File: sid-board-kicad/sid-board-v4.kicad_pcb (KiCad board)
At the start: 2 copper layers, 52 parts, among them J1 SPI + UART, J2 USB_B_Micro, Q1 BSS138, Q2 BSS138, SW1 SW_EN, SW2 SW_FLASH, U1 SC16IS762IBS, U2 MCP1703A-3302_SOT223, U3 SN65HVD232, U4 SN65HVD232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

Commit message: Layer 4 stuff
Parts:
- removed the C8 at (139.6, 90.9)
- removed the C8 at (147.4, 90.9)
- removed D1: LED7, LED_SMD:LED_0805_2012Metric_Pad1.15x1.40mm_HandSolder
- removed D2: LED6, LED_SMD:LED_0805_2012Metric_Pad1.15x1.40mm_HandSolder
- removed D3: LED5, LED_SMD:LED_0805_2012Metric_Pad1.15x1.40mm_HandSolder
- removed D4: LED4, LED_SMD:LED_0805_2012Metric_Pad1.15x1.40mm_HandSolder
- removed D5: LED3, LED_SMD:LED_0805_2012Metric_Pad1.15x1.40mm_HandSolder
- removed D6: LED2, LED_SMD:LED_0805_2012Metric_Pad1.15x1.40mm_HandSolder
- removed D7: LED1, LED_SMD:LED_0805_2012Metric_Pad1.15x1.40mm_HandSolder
- removed D8: LED0, LED_SMD:LED_0805_2012Metric_Pad1.15x1.40mm_HandSolder
- removed J1: SPI + UART, Connector_PinHeader_2.00mm:PinHeader_2x05_P2.00mm_Vertical
- removed R18: 1K, Resistor_SMD:R_0805_2012Metric_Pad1.15x1.40mm_HandSolder
- added C8: 1uF, Capacitor_SMD:C_0805_2012Metric_Pad1.15x1.40mm_HandSolder, F.Cu at (108.6, 81.3)
- C2, C5, C9, D10, D11, U2, U3, U4, U7: moved to F.Cu
- moved I-BUS1 71.2 mm to (117.5, 141.0), turned to 90 degrees
- moved H3 69.7 mm to (109.2, 71.1)
- moved H1 65.5 mm to (154.9, 116.8)
- moved R5 63.1 mm to (201.8, 94.9), turned to 0 degrees
- moved R4 56.1 mm to (194.7, 100.9), turned to 0 degrees
- moved H2 56.0 mm to (154.9, 71.1)
- moved C6 55.7 mm to (194.8, 106.8)
- moved U7 55.1 mm to (127.0, 138.4), turned to 180 degrees
- moved R6 52.2 mm to (190.2, 90.0)
- moved R2 50.8 mm to (190.1, 105.9), turned to 0 degrees
- moved J2 50.5 mm to (132.1, 119.4), turned to 0 degrees
- moved C5 49.4 mm to (126.8, 133.3)
- moved R3 46.1 mm to (185.3, 109.0), turned to 0 degrees
- moved Q2 44.7 mm to (199.4, 104.6)
- moved SW1 43.9 mm to (86.4, 106.0), turned to 0 degrees
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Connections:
- ICM1 pad 1: (no net) -> Net-(ICM1-Pad1)
- ICM1 pad 11: (no net) -> Net-(ICM1-Pad11)
- ICM1 pad 12: (no net) -> Net-(ICM1-Pad12)
- ICM1 pad 4: (no net) -> Net-(ICM1-Pad4)
- ICM1 pad 7: (no net) -> Net-(ICM1-Pad7)
- ICM1 pad 8: (no net) -> Net-(ICM1-Pad8)
- J2 pad 4: (no net) -> Net-(J2-Pad4)
- SID1 pad 1: (no net) -> Net-(SID1-Pad1)
- SID1 pad 11: (no net) -> Net-(SID1-Pad11)
- SID1 pad 12: (no net) -> Net-(SID1-Pad12)
- SID1 pad 4: (no net) -> Net-(SID1-Pad4)
- SID1 pad 7: (no net) -> Net-(SID1-Pad7)
- SID1 pad 8: (no net) -> Net-(SID1-Pad8)
- U1 pad 15: (no net) -> Net-(U1-Pad15)
- U1 pad 16: (no net) -> Net-(U1-Pad16)
- U1 pad 17: (no net) -> Net-(U1-Pad17)
- U1 pad 18: (no net) -> Net-(U1-Pad18)
- U1 pad 19: (no net) -> Net-(U1-Pad19)
- U1 pad 2: (no net) -> Net-(U1-Pad2)
- U1 pad 20: (no net) -> Net-(U1-Pad20)
- U1 pad 24: (no net) -> Net-(U1-Pad24)
- U1 pad 25: (no net) -> Net-(U1-Pad25)
- U1 pad 26: (no net) -> Net-(U1-Pad26)
- U1 pad 27: (no net) -> Net-(U1-Pad27)
- U1 pad 30: (no net) -> Net-(U1-Pad30)
- U1 pad 31: (no net) -> Net-(U1-Pad31)
- U1 pad 4: (no net) -> Net-(U1-Pad4)
- U1 pad 6: (no net) -> Net-(U1-Pad6)
- U3 pad 5: (no net) -> Net-(U3-Pad5)
- U3 pad 8: (no net) -> Net-(U3-Pad8)
- U4 pad 5: (no net) -> Net-(U4-Pad5)
- U4 pad 8: (no net) -> Net-(U4-Pad8)
- U5 pad 1: (no net) -> Net-(U5-Pad1)
- U5 pad 10: (no net) -> Net-(U5-Pad10)
- U5 pad 11: (no net) -> Net-(U5-Pad11)
- U5 pad 12: (no net) -> Net-(U5-Pad12)
- U5 pad 13: (no net) -> Net-(U5-Pad13)
- U5 pad 14: (no net) -> Net-(U5-Pad14)
- U5 pad 15: (no net) -> Net-(U5-Pad15)
- U5 pad 16: (no net) -> Net-(U5-Pad16)
- U5 pad 17: (no net) -> Net-(U5-Pad17)
- U5 pad 2: (no net) -> Net-(U5-Pad2)
- U5 pad 20: (no net) -> Net-(U5-Pad20)
- U5 pad 21: (no net) -> Net-(U5-Pad21)
- U5 pad 22: (no net) -> Net-(U5-Pad22)
- U5 pad 23: (no net) -> Net-(U5-Pad23)
- U5 pad 27: (no net) -> Net-(U5-Pad27)
- U5 pad 7: (no net) -> Net-(U5-Pad7)
- U5 pad 9: (no net) -> Net-(U5-Pad9)
- U6 pad 17: (no net) -> Net-(U6-Pad17)
- U6 pad 18: (no net) -> Net-(U6-Pad18)
- U6 pad 19: (no net) -> Net-(U6-Pad19)
- U6 pad 20: (no net) -> Net-(U6-Pad20)
- U6 pad 21: (no net) -> Net-(U6-Pad21)
- U6 pad 22: (no net) -> Net-(U6-Pad22)
- U6 pad 27: (no net) -> Net-(U6-Pad27)
- U6 pad 28: (no net) -> Net-(U6-Pad28)
- U6 pad 30: (no net) -> Net-(U6-Pad30)
- U6 pad 31: (no net) -> Net-(U6-Pad31)
- U6 pad 32: (no net) -> Net-(U6-Pad32)
- U6 pad 33: (no net) -> Net-(U6-Pad33)
- U6 pad 37: (no net) -> Net-(U6-Pad37)
- U6 pad 4: (no net) -> Net-(U6-Pad4)
- U6 pad 5: (no net) -> Net-(U6-Pad5)
- U6 pad 6: (no net) -> Net-(U6-Pad6)
- U6 pad 7: (no net) -> Net-(U6-Pad7)
- U7 pad 5: (no net) -> Net-(U7-Pad5)
- U7 pad 8: (no net) -> Net-(U7-Pad8)
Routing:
- net GND: track 0.00 -> 24.4 mm, vias 0 -> 6
- net +3V3: track 0.00 -> 22.8 mm, vias 0 -> 7
- net Net-(D11-Pad2): track 0.00 -> 11.5 mm
- net VCC: track 0.00 -> 8.54 mm
- added copper zone on In1.Cu, net +3V3
- added copper zone on In2.Cu, net GND
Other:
- board outline added: 55.9 x 55.9 mm
- copper layers 2 -> 4

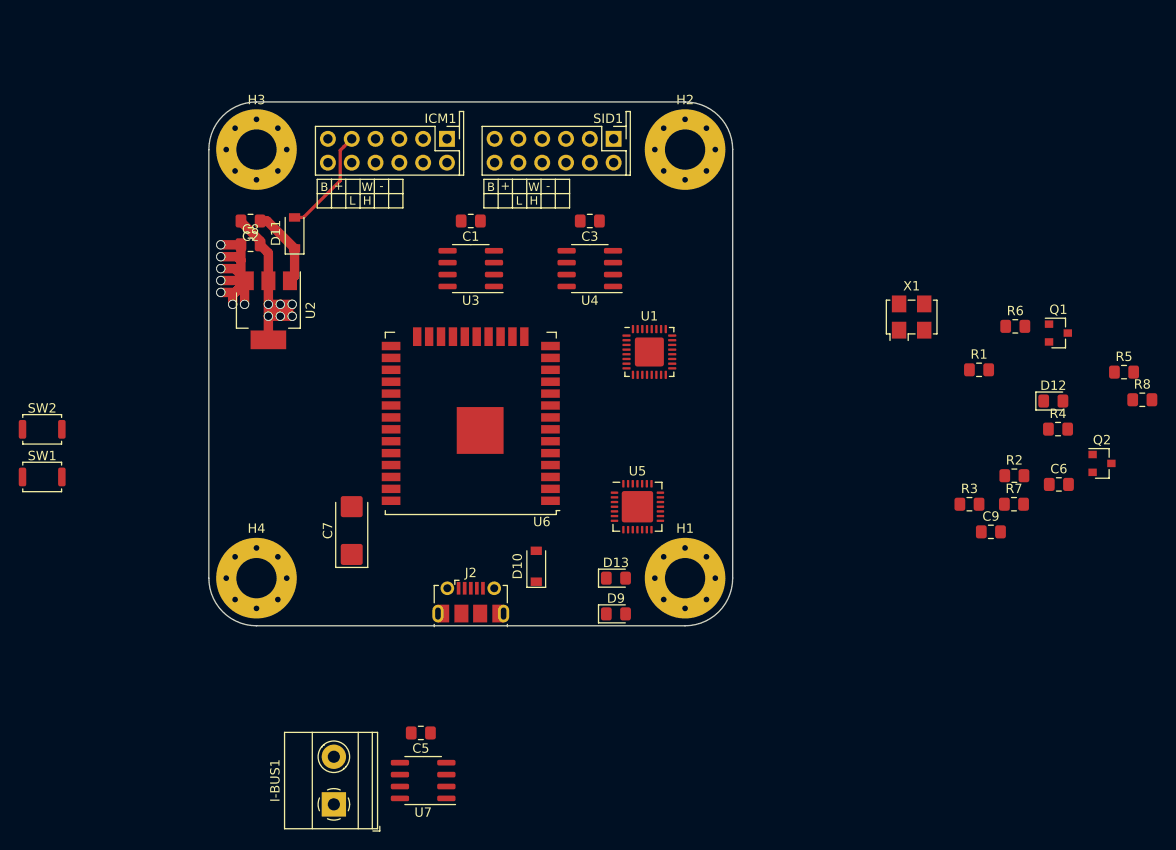
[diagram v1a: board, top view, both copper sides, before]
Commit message: Layer 4 experiments
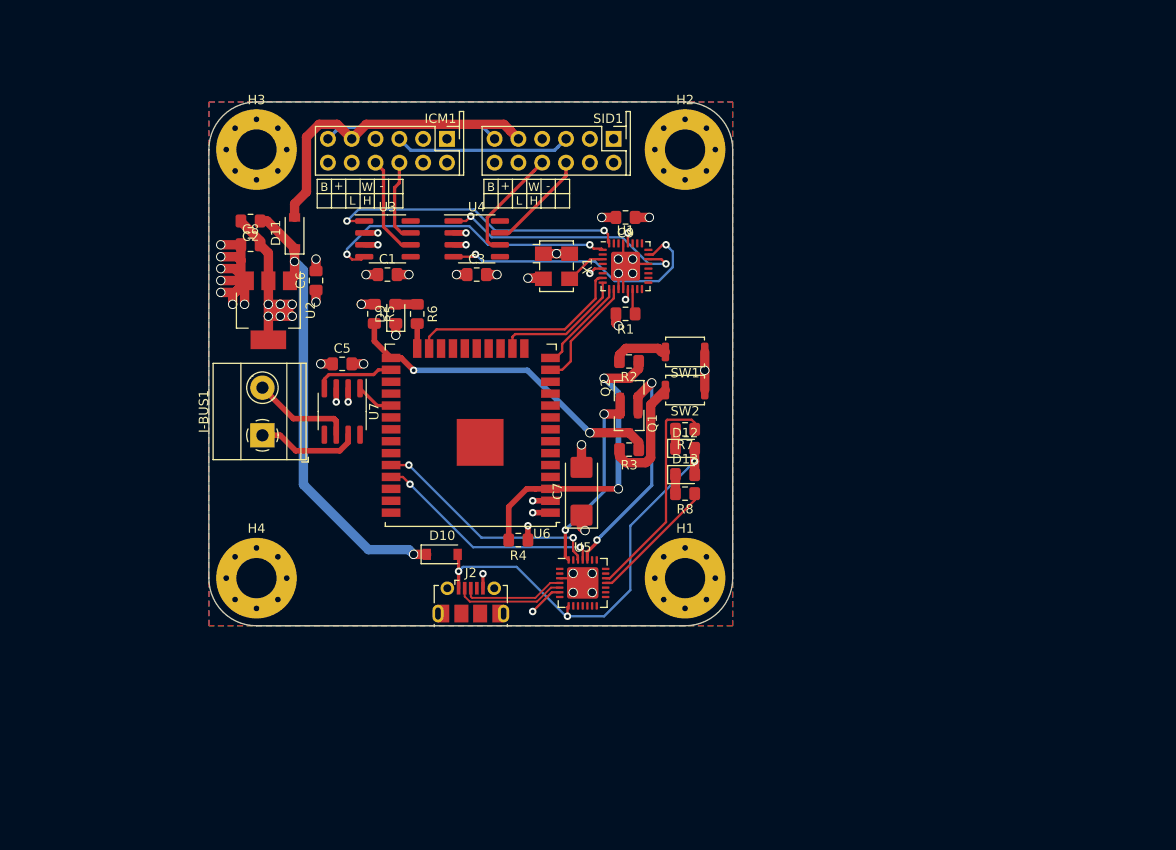
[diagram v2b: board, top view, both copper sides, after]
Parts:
- moved C6 82.2 mm to (115.6, 85.1), turned to 90 degrees
- moved R5 80.2 mm to (121.8, 88.6), turned to 270 degrees
- moved SW1 69.9 mm to (154.9, 92.7), turned to 180 degrees
- moved SW2 68.7 mm to (154.9, 96.8), turned to 180 degrees
- moved R6 63.8 mm to (126.4, 88.7), turned to 270 degrees
- moved R4 58.8 mm to (137.2, 112.8), turned to 180 degrees
- moved C9 51.4 mm to (148.6, 78.4), turned to 180 degrees
- moved Q2 51.1 mm to (149.0, 96.5), turned to 90 degrees
- moved R8 49.8 mm to (154.9, 107.8), turned to 180 degrees
- moved Q1 46.8 mm to (149.0, 100.3), turned to 270 degrees
- moved R2 42.9 mm to (149.0, 93.7), turned to 180 degrees
- moved U7 40.3 mm to (118.4, 99.1), turned to 270 degrees
- moved C5 40.3 mm to (118.4, 94.0), turned to 0 degrees
- moved I-BUS1 40.1 mm to (109.9, 101.6)
- moved D9 39.7 mm to (124.1, 88.6), turned to 90 degrees
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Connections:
- U1 pad 33: (no net) -> GND
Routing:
- net VBUS: track 0.00 -> 46.0 mm, vias 0 -> 3
- net VCC: track 8.54 -> 49.0 mm, vias 0 -> 2
- net IO0: track 0.00 -> 35.3 mm, vias 0 -> 2
- net GND: track 24.4 -> 59.3 mm, vias 6 -> 28
- net EN: track 0.00 -> 33.3 mm, vias 0 -> 2
- net TXA: track 0.00 -> 32.3 mm, vias 0 -> 2
- net RXA: track 0.00 -> 32.1 mm, vias 0 -> 2
- net +3V3: track 22.8 -> 53.3 mm, vias 7 -> 25
- net RXB: track 0.00 -> 30.3 mm, vias 0 -> 2
- net TXB: track 0.00 -> 27.1 mm, vias 0 -> 2
- net RTS: track 0.00 -> 25.7 mm, vias 0 -> 2
- net RX_ESP32: track 0.00 -> 25.2 mm, vias 0 -> 2
- net TX_ESP32: track 0.00 -> 24.8 mm, vias 0 -> 2
- net Net-(R7-Pad1): track 0.00 -> 23.6 mm
- net CS: track 0.00 -> 23.5 mm
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- added copper zone on B.Cu, net GND
- added copper zone on F.Cu, net GND

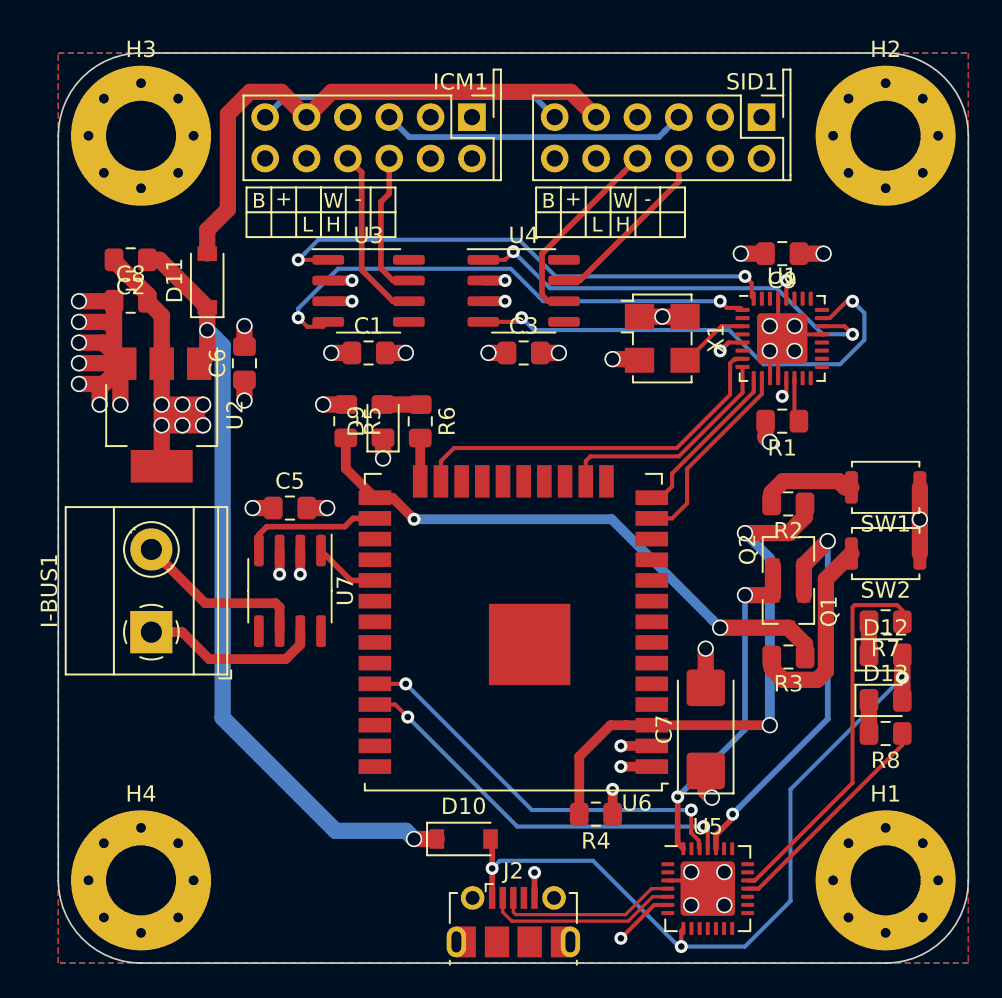
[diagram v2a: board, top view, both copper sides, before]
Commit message: Added USBC port which I know exists
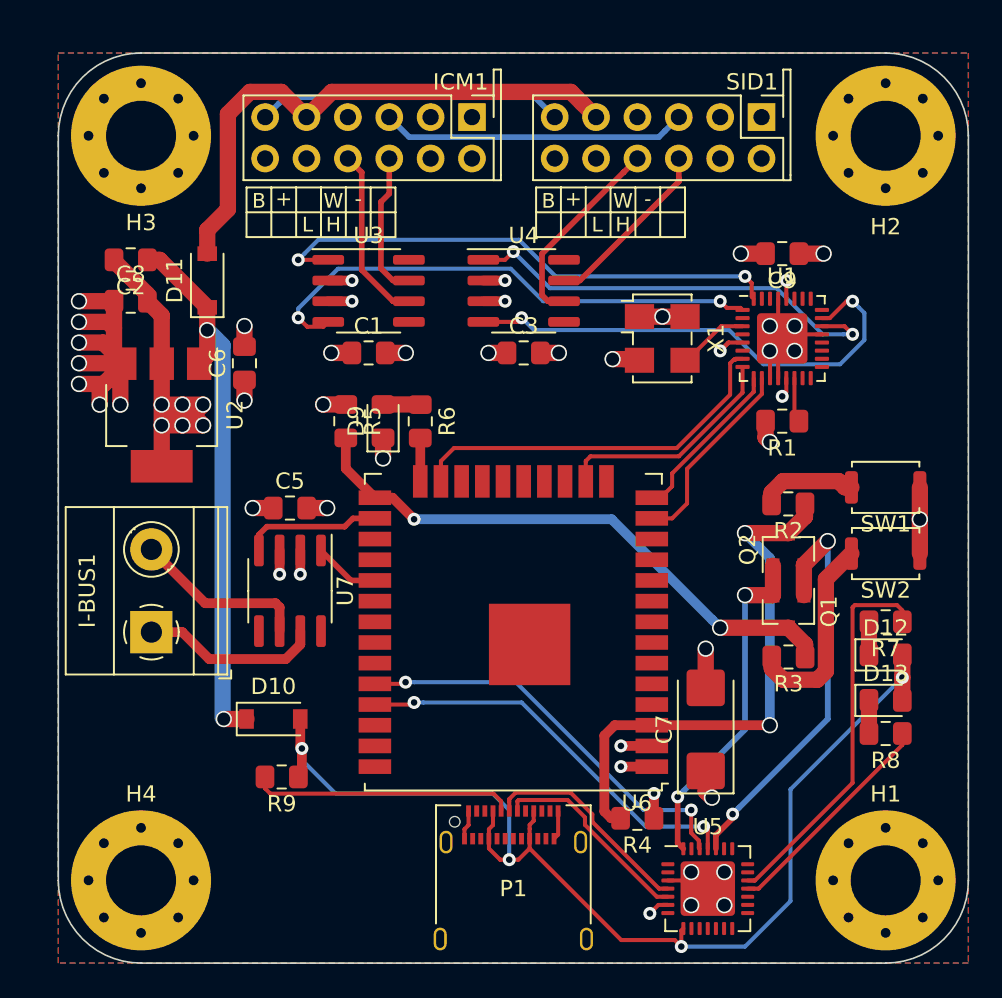
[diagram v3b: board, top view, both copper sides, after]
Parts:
- removed J2: USB_B_Micro, Connector_USB:USB_Micro-B_Molex-105017-0001
- added P1: USB_C_Plug_USB2.0, Connector_USB:USB_C_Receptacle_Amphenol_12401610E4-2A, F.Cu at (132.1, 117.6)
- added R9: 56k, Resistor_SMD:R_0805_2012Metric_Pad1.15x1.40mm_HandSolder, F.Cu at (117.9, 110.5)
- moved D10 13.8 mm to (117.3, 106.9)
- moved R4 2.55 mm to (139.7, 113.0)
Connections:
- U1 pad 33: GND -> (no net)
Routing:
- net VBUS: track 46.0 -> 69.7 mm, vias 3 -> 4
- net Net-(P1-PadA5): track 0.00 -> 16.1 mm
- net VCC: track 49.0 -> 34.1 mm
- net +3V3: track 53.3 -> 50.9 mm
- net USB_DP: track 11.1 -> 13.3 mm
- net GND: track 59.3 -> 61.4 mm, vias 28 -> 27
- net USB_DM: track 11.9 -> 12.6 mm

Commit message: Formatting
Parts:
- added REF**: USB_C_Receptacle_Amphenol_12401548E4-2A, Connector_USB:USB_C_Receptacle_Amphenol_12401548E4-2A, F.Cu at (167.1, 117.6)
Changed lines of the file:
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@@
     (tracks 480)
     (zones 0)
-    (modules 42)
+    (modules 43)
     (nets 117)
   )
@@
     (add_net XTAL1)
   )
+  (module Connector_USB:USB_C_Receptacle_Amphenol_12401548E4-2A (layer F.Cu)
+    (at 167.132 117.602)
+    (descr "USB TYPE C, RA RCPT PCB, Hybrid, https://www.amphenolcanada.com/StockAvailabilityPrice.aspx?From=&PartNum=12401548E4%7e2A")
+    (tags "USB C Type-C Receptacle Hybrid")
+    (attr smd)
+    (fp_text reference REF** (at 0 -6.36) (layer F.SilkS)
+      (effects (font (size 1 1) (thickness 0.15)))
+    )
+    (fp_text value USB_C_Receptacle_Amphenol_12401548E4-2A (at 0 6.14) (layer F.Fab)
+      (effects (font (size 1 1) (thickness 0.15)))
+    )
+    (fp_line (start -4.6 5.23) (end -4.6 -5.22) (layer F.Fab) (width 0.1))
+    (fp_line (start -4.6 -5.22) (end 4.6 -5.22) (layer F.Fab) (width 0.1))
+    (fp_line (start -4.75 -5.37) (end -3.25 -5.37) (layer F.SilkS) (width 0.12))
+    (fp_line (start -4.75 -5.37) (end -4.75 1.89) (layer F.SilkS) (width 0.12))
+    (fp_line (start 4.75 -5.37) (end 4.75 1.89) (layer F.SilkS) (width 0.12))
+    (fp_line (start 3.25 -5.37) (end 4.75 -5.37) (layer F.SilkS) (width 0.12))
+    (fp_line (start -4.6 5.23) (end 4.6 5.23) (layer F.Fab) (width 0.1))
+    (fp_line (start 4.6 5.23) (end 4.6 -5.22) (layer F.Fab) (width 0.1))
+    (fp_line (start -5.39 -5.87) (end 5.39 -5.87) (layer F.CrtYd) (width 0.05))
+    (fp_line (start 5.39 -5.87) (end 5.39 5.73) (layer F.CrtYd) (width 0.05))
+    (fp_line (start 5.39 5.73) (end -5.39 5.73) (layer F.CrtYd) (width 0.05))
+    (fp_line (start -5.39 5.73) (end -5.39 -5.87) (layer F.CrtYd) (width 0.05))
+    (fp_text user %R (at 0 0) (layer F.Fab)
+      (effects (font (size 1 1) (thickness 0.1)))
+    )
+    (pad B11 thru_hole circle (at -2.4 -3.01) (size 0.65 0.65) (drill 0.4) (layers *.Cu *.Mask))
+    (pad B10 thru_hole circle (at -1.6 -3.01) (size 0.65 0.65) (drill 0.4) (layers *.Cu *.Mask))
+    (pad B8 thru_hole circle (at -0.8 -3.01) (size 0.65 0.65) (drill 0.4) (layers *.Cu *.Mask))
+    (pad B5 thru_hole circle (at 0.8 -3.01) (size 0.65 0.65) (drill 0.4) (layers *.Cu *.Mask))
+    (pad B3 thru_hole circle (at 1.6 -3.01) (size 0.65 0.65) (drill 0.4) (layers *.Cu *.Mask))
+    (pad B2 thru_hole circle (at 2.4 -3.01) (size 0.65 0.65) (drill 0.4) (layers *.Cu *.Mask))
+    (pad B12 thru_hole circle (at -2.8 -3.71) (size 0.65 0.65) (drill 0.4) (layers *.Cu *.Mask))
+    (pad B9 thru_hole circle (at -1.2 -3.71) (size 0.65 0.65) (drill 0.4) (layers *.Cu *.Mask))
+    (pad B7 thru_hole circle (at -0.4 -3.71) (size 0.65 0.65) (drill 0.4) (layers *.Cu *.Mask))
+    (pad B6 thru_hole circle (at 0.4 -3.71) (size 0.65 0.65) (drill 0.4) (layers *.Cu *.Mask))
+    (pad B4 thru_hole circle (at 1.2 -3.71) (size 0.65 0.65) (drill 0.4) (layers *.Cu *.Mask))
+    (pad B1 thru_hole circle (at 2.8 -3.71) (size 0.65 0.65) (drill 0.4) (layers *.Cu *.Mask))
+    (pad "" np_thru_hole circle (at -3.6 -4.36) (size 0.65 0.65) (drill 0.65) (layers *.Cu *.Mask))
+    (pad "" np_thru_hole oval (at 3.6 -4.36) (size 0.95 0.65) (drill oval 0.95 0.65) (layers *.Cu *.Mask))
+    (pad S1 thru_hole oval (at -4.49 2.84) (size 0.8 1.4) (drill oval 0.5 1.1) (layers *.Cu *.Mask))
+    (pad S1 thru_hole oval (at 4.49 2.84) (size 0.8 1.4) (drill oval 0.5 1.1) (layers *.Cu *.Mask))
+    (pad S1 thru_hole oval (at 4.13 -3.11) (size 0.8 1.4) (drill oval 0.5 1.1) (layers *.Cu *.Mask))
+    (pad A11 smd rect (at 2.25 -5.02) (size 0.3 0.7) (layers F.Cu F.Paste F.Mask))
+    (pad A8 smd rect (at 0.75 -5.02) (size 0.3 0.7) (layers F.Cu F.Paste F.Mask))
+    (pad A9 smd rect (at 1.25 -5.02) (size 0.3 0.7) (layers F.Cu F.Paste F.Mask))
+    (pad A10 smd rect (at 1.75 -5.02) (size 0.3 0.7) (layers F.Cu F.Paste F.Mask))
+    (pad A12 smd rect (at 2.75 -5.02) (size 0.3 0.7) (layers F.Cu F.Paste F.Mask))
+    (pad A7 smd rect (at 0.25 -5.02) (size 0.3 0.7) (layers F.Cu F.Paste F.Mask))
+    (pad A6 smd rect (at -0.25 -5.02) (size 0.3 0.7) (layers F.Cu F.Paste F.Mask))
+    (pad A5 smd rect (at -0.75 -5.02) (size 0.3 0.7) (layers F.Cu F.Paste F.Mask))
+    (pad A4 smd rect (at -1.25 -5.02) (size 0.3 0.7) (layers F.Cu F.Paste F.Mask))
+    (pad A3 smd rect (at -1.75 -5.02) (size 0.3 0.7) (layers F.Cu F.Paste F.Mask))
+    (pad A2 smd rect (at -2.25 -5.02) (size 0.3 0.7) (layers F.Cu F.Paste F.Mask))
+    (pad A1 smd rect (at -2.75 -5.02) (size 0.3 0.7) (layers F.Cu F.Paste F.Mask))
+    (pad S1 thru_hole oval (at -4.13 -3.11) (size 0.8 1.4) (drill oval 0.5 1.1) (layers *.Cu *.Mask))
+    (model ${KISYS3DMOD}/Connector_USB.3dshapes/USB_C_Receptacle_Amphenol_12401548E4-2A.wrl
+      (at (xyz 0 0 0))
+      (scale (xyz 1 1 1))
+      (rotate (xyz 0 0 0))
+    )
+  )
   (module Capacitor_SMD:C_0805_2012Metric_Pad1.15x1.40mm_HandSolder (layer F.Cu)
